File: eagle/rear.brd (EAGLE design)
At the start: 22 x 22 mm, 11 parts, among them T1 BC846, T2 BC846, T3 BC846

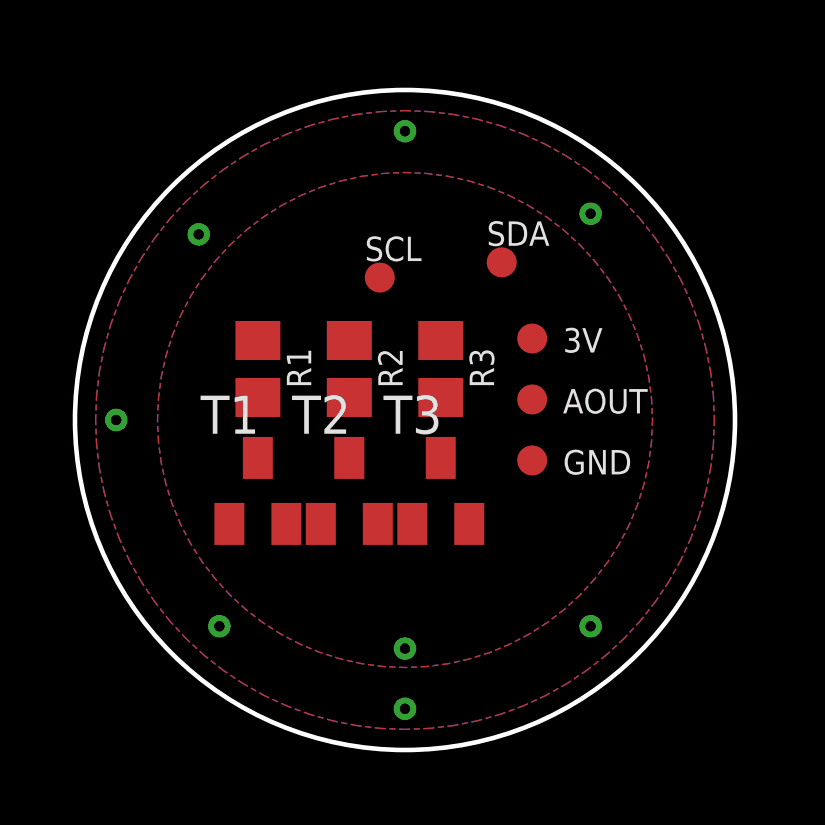
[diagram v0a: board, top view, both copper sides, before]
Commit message: Updated probe and rear eagle files
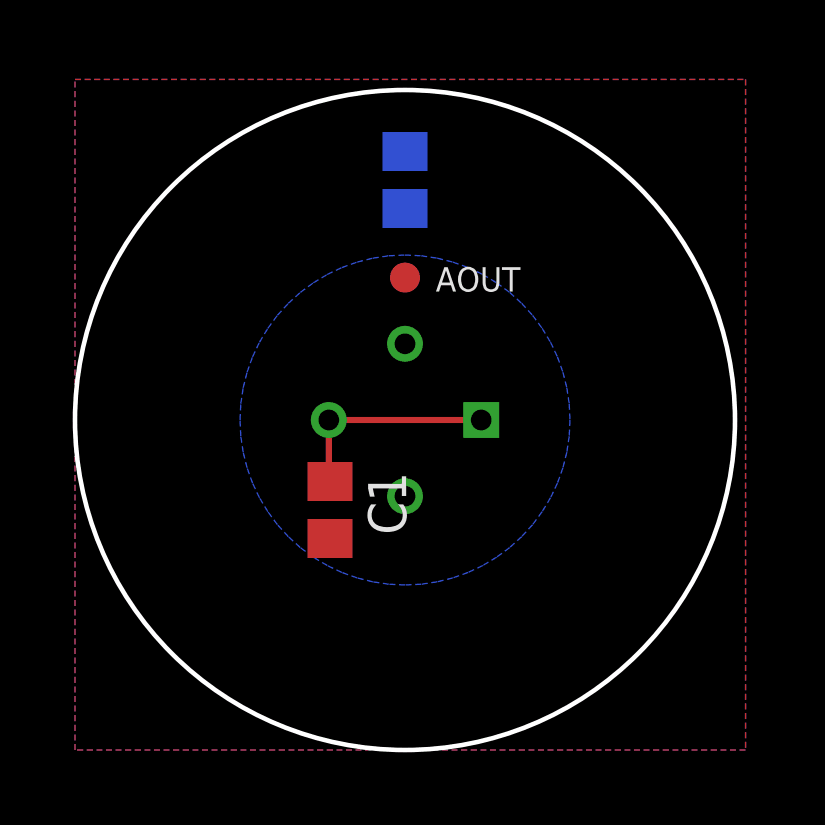
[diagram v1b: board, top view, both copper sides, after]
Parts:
- removed 3V, GND, SCL, SDA: TPTP10R, testpad:TP10R
- removed R1, R2, R3: (no value), resistor:R0805
- removed T1, T2, T3: BC846, transistor:SOT23
- added C1: 0.1uF, resistor:C0805
- added C2: ?uF, resistor:C0805
- added U1: MLX90614ESF-BAA-000-TU, MLX90614ESF-BAA-000-TU:TO254P942H425-4
- moved AOUT 5.87 mm to (11.0, 15.7)
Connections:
- removed net N$1: T1.2, T2.1
- removed net N$2: T2.2, T3.1
- removed net N$3: R1.1, T1.3
- removed net N$4: R2.1, T2.3
- removed net SCL: SCL.TP
- net 3V: now also C1.1, U1.1, U1.3; no longer 3V.TP, R1.2, R2.2, R3.2
- net ANT: now also C2.1; no longer T1.1
- net AOUT: now also C2.2; no longer R3.1, T3.3
- net GND: now also C1.2, U1.4; no longer GND.TP, T3.2
- net SDA: now also U1.2; no longer SDA.TP
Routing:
- net 3V: track 0.00 -> 7.15 mm
- removed copper zone on layer 1, net ANT

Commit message: new pcbs
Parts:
- removed C2: ?uF, resistor:C0805
- added R1: 10k, rcl:R0805
- renumbered AOUT to ANT
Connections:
- removed net AOUT: ANT.TP, C2.2
- new net SCL: R1.1, U1.1
- net 3V: now also R1.2; no longer U1.1
- net ANT: now also ANT.TP; no longer C2.1
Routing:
- net ANT: track 0.00 -> 2.75 mm, vias 0 -> 1
- net SCL: track 0.00 -> 2.07 mm
- net 3V: track 7.15 -> 7.89 mm
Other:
- board text added: "3V"
- board text added: "GND"
- board text added: "SCL"
- board text added: "SDA"
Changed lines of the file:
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@@
 <plain>
 <circle x="11" y="11" radius="11" width="0.1524" layer="20"/>
+<text x="6.5" y="12" size="0.8128" layer="25">3V</text>
+<text x="14.5" y="12" size="0.8128" layer="25">SCL</text>
+<text x="10" y="9.5" size="0.8128" layer="25">SDA</text>
+<text x="12" y="14.5" size="0.8128" layer="25">GND</text>
 </plain>
 <attributes>
@@
 </autorouter>
 <elements>
-<element name="AOUT" library="testpad" library_urn="urn:adsk.eagle:library:385" package="TP10R" package3d_urn="urn:adsk.eagle:package:27959/1" value="TPTP10R" x="11" y="15.748" smashed="yes">
-<attribute name="NAME" x="12.0239" y="15.2819" size="0.8128" layer="25"/>
+<element name="ANT" library="testpad" library_urn="urn:adsk.eagle:library:385" package="TP10R" package3d_urn="urn:adsk.eagle:package:27959/1" value="TPTP10R" x="11" y="15.748" smashed="yes">
+<attribute name="NAME" x="9.0239" y="16.7819" size="0.8128" layer="25"/>
 <attribute name="POPULARITY" value="3" x="11" y="15.748" size="1.778" layer="27" display="off"/>
 <attribute name="TP_SIGNAL_NAME" value="" x="11" y="15.748" size="1.778" layer="27" display="off"/>
@@
 </element>
 <element name="C1" library="resistor" library_urn="urn:adsk.eagle:library:348" package="C0805" package3d_urn="urn:adsk.eagle:package:23617/2" value="0.1uF" x="8.5" y="8" smashed="yes" rot="R270">
-<attribute name="NAME" x="9.77" y="9.27" size="1.27" layer="25" rot="R270"/>
-<attribute name="VALUE" x="5.96" y="9.27" size="1.27" layer="27" rot="R270"/>
-</element>
-<element name="C2" library="resistor" library_urn="urn:adsk.eagle:library:348" package="C0805" package3d_urn="urn:adsk.eagle:package:23617/2" value="?uF" x="11" y="19" smashed="yes" rot="MR270">
-<attribute name="NAME" x="9.73" y="20.27" size="1.27" layer="26" rot="MR270"/>
-<attribute name="VALUE" x="13.54" y="20.27" size="1.27" layer="28" rot="MR270"/>
+<attribute name="VALUE" x="5.5" y="10.5" size="1.27" layer="27" rot="R270"/>
+</element>
+<element name="R1" library="rcl" library_urn="urn:adsk.eagle:library:334" package="R0805" package3d_urn="urn:adsk.eagle:package:23553/2" value="10k" x="13.5" y="8" smashed="yes" rot="R270">
+<attribute name="POPULARITY" value="86" x="13.5" y="8" size="1.778" layer="27" rot="R270" display="off"/>
+<attribute name="SPICEPREFIX" value="R" x="13.5" y="8" size="1.778" layer="27" rot="R270" display="off"/>
+<attribute name="VALUE" x="14.96" y="9.635" size="1.27" layer="27" rot="R270"/>
 </element>
 </elements>
@@
 <vertex x="22.352" y="0"/>
 </polygon>
-<contactref element="C2" pad="1"/>
+<contactref element="ANT" pad="TP"/>
+<polygon width="0.2032" layer="16" rank="5">
+<vertex x="-0.5" y="-0.5"/>
+<vertex x="-0.5" y="23"/>
+<vertex x="23" y="23"/>
+<vertex x="23" y="-0.5"/>
+</polygon>
+<wire x1="11" y1="15.748" x2="11" y2="18.5" width="0.2032" layer="1"/>
+<via x="11" y="18.5" extent="1-16" drill="0.35"/>
 </signal>
 <signal name="3V">
-<contactref element="U1" pad="1"/>
 <contactref element="U1" pad="3"/>
 <contactref element="C1" pad="1"/>
 <wire x1="8.5" y1="8.95" x2="8.46" y2="8.99" width="0.2032" layer="1"/>
 <wire x1="8.46" y1="8.99" x2="8.46" y2="11" width="0.2032" layer="1"/>
-<wire x1="8.46" y1="11" x2="13.54" y2="11" width="0.2032" layer="1"/>
+<contactref element="R1" pad="2"/>
+<wire x1="8.5" y1="8.95" x2="8.55" y2="8.95" width="0.2032" layer="1"/>
+<wire x1="8.55" y1="8.95" x2="10.5" y2="7" width="0.2032" layer="1"/>
+<wire x1="10.5" y1="7" x2="13.45" y2="7" width="0.2032" layer="1"/>
+<wire x1="13.45" y1="7" x2="13.5" y2="7.05" width="0.2032" layer="1"/>
 </signal>
 <signal name="GND">
@@
 <contactref element="C1" pad="2"/>
 </signal>
-<signal name="AOUT">
-<contactref element="AOUT" pad="TP"/>
-<contactref element="C2" pad="2"/>
-<wire x1="11" y1="15.748" x2="11" y2="18.05" width="0" layer="19" extent="1-16"/>
-</signal>
 <signal name="SDA">
 <contactref element="U1" pad="2"/>
 </signal>
+<signal name="SCL">
+<contactref element="U1" pad="1"/>
+<contactref element="R1" pad="1"/>
+<wire x1="13.5" y1="8.95" x2="13.5" y2="10.96" width="0.2032" layer="1"/>
+<wire x1="13.5" y1="10.96" x2="13.54" y2="11" width="0.2032" layer="1"/>
+</signal>
 </signals>

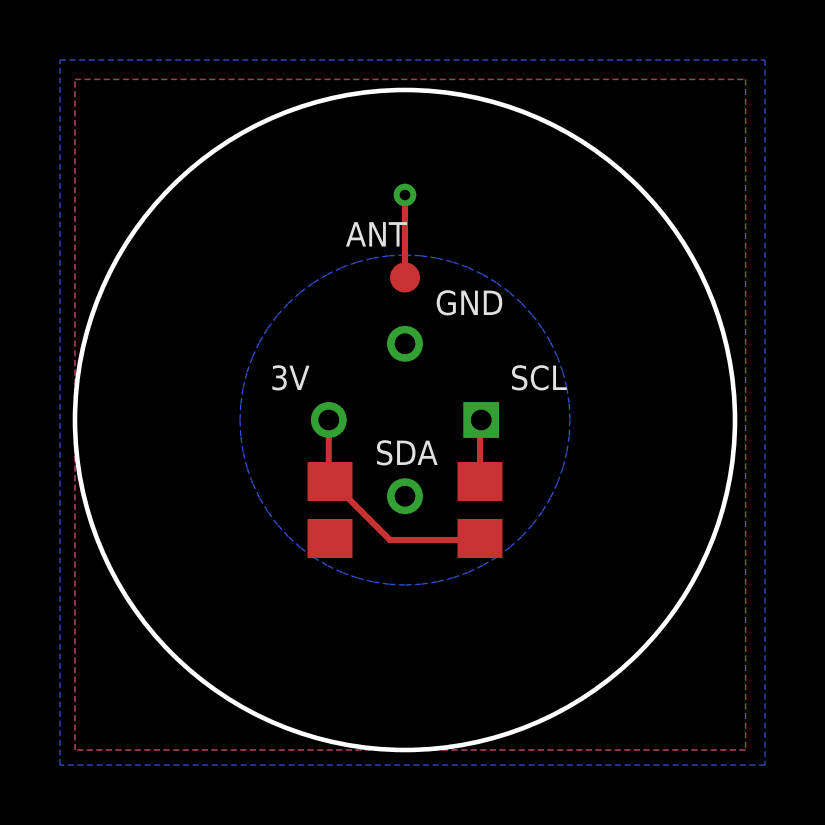
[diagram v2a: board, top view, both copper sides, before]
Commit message: added encoder to rear pcb
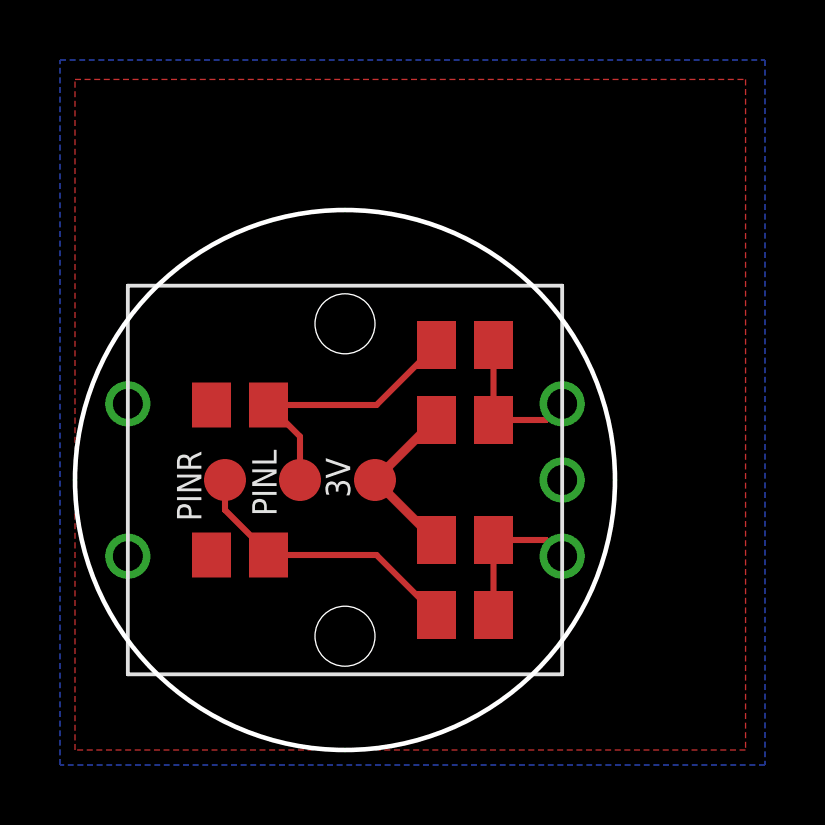
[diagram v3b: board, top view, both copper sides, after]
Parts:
- removed ANT: TPTP10R, testpad:TP10R
- removed R1: 10k, rcl:R0805
- removed U1: MLX90614ESF-BAA-000-TU, MLX90614ESF-BAA-000-TU:TO254P942H425-4
- added 3V, PINL, PINR: TPTP14R, testpad:TP14R
- added C2: 0.1u, resistor:C0805
- added R10, R5, R8, R9: 10k, resistor:M0805
- added U$1: ENCODER, general:ENCODER
- C1: value 0.1uF -> 0.1u
- moved C1 4.61 mm to (5.50, 11.5), turned to 180 degrees
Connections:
- removed net ANT: ANT.TP
- removed net SCL: R1.1, U1.1
- removed net SDA: U1.2
- new net ENCL: R5.2, R8.1, U$1.L
- new net ENCPINL: C1.1, PINL.TP, R5.1
- new net ENCPINR: C2.1, PINR.TP, R10.1
- new net ENCR: R10.2, R9.1, U$1.R
- net 3V: now also 3V.TP, R8.2, R9.2; no longer C1.1, R1.2, U1.3
- net GND: now also C2.2, U$1.C; no longer U1.4
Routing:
- net ENCPINR: track 0.00 -> 9.55 mm
- net ENCPINL: track 0.00 -> 9.36 mm
- net ENCR: track 0.00 -> 5.01 mm
- net ENCL: track 0.00 -> 5.01 mm
- net ANT: track 2.75 -> 0.00 mm, vias 1 -> 0
- net 3V: track 7.89 -> 5.76 mm
- net SCL: track 2.07 -> 0.00 mm
- removed copper zone on layer 16, net ANT
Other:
- board size 22 x 22 mm -> 18 x 18 mm
- board text removed: "3V"
- board text removed: "GND"
- board text removed: "SCL"
- board text removed: "SDA"
